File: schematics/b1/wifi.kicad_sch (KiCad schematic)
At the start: 0 parts

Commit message: Updated Wi-Fi block.
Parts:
- added C18: 1 mF, symbol Device:C_Polarized
- added J1: Conn_01x06_Pin, symbol Connector:Conn_01x06_Pin
- added R26, R27, R28, R29, R30: 10k, symbol Device:R
- added SW2, SW3: SW_Push, symbol Switch:SW_Push
- added U6: ESP-12F, RF_Module:ESP-12E, symbol RF_Module:ESP-12F
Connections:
- new net: R27.2, U6.3 (EN)
- new net: R26.1, SW2.2, U6.1 (~{RST})
- new net: J1.4 (TX), U6.21 (GPIO3/RXD)
- new net: J1.5 (RX), U6.22 (GPIO1/TXD)
- new net: R29.1, U6.17 (GPIO2)
- new net CS: R30.1, U6.16 (GPIO15)
- new net GND: C18.2, J1.1 (GND), R30.2, SW2.1, SW3.1, U6.15 (GND)
- new net GPIO0: R28.2, SW3.2, U6.18 (GPIO0)
- new net GPIO4: U6.19 (GPIO4)
- new net GPIO5: U6.20 (GPIO5)
- new net MOSI: U6.7 (GPIO13)
- new net SCLK: U6.5 (GPIO14)
- new net VCC: C18.1, R26.2, R27.1, R28.1, R29.2, U6.8 (VCC)
- no-connect marks 0 -> 12
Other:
- note added: "An extremely beefy capacitor is needed so that VCC doesn't drop too low at boot time, or else the ESP-12F will crash and enter an idle state."
- note added: "If this is held down while the module is booting, then it will enter flash mode."
- note added: "If this is pushed, then the module will reset."

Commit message: Updated index page.
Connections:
- net RX: now reaches J1.4 (TX), U6.21 (GPIO3/RXD)
- net TX: now reaches J1.5 (RX), U6.22 (GPIO1/TXD)
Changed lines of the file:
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@@
     (comment 3 "A B1 (Badger One) node is the core hardware unit of the Badger sytem. It handles card")
+  )
+  (junction (at 115.57 46.99) (diameter 0) (color 0 0 0 0)
   )
   (junction (at 95.25 34.29) (diameter 0) (color 0 0 0 0)
   )
   (junction (at 137.16 57.15) (diameter 0) (color 0 0 0 0)
+  )
+  (junction (at 113.03 44.45) (diameter 0) (color 0 0 0 0)
   )
   (junction (at 118.11 80.01) (diameter 0) (color 0 0 0 0)
@@
     (stroke (width 0) (type default))
   )
+  (wire (pts (xy 113.03 44.45) (xy 118.11 44.45))
+    (stroke (width 0) (type default))
+  )
   (wire (pts (xy 95.25 34.29) (xy 95.25 52.07))
     (stroke (width 0) (type default))
@@
     (stroke (width 0) (type default))
   )
+  (wire (pts (xy 113.03 44.45) (xy 113.03 36.83))
+    (stroke (width 0) (type default))
+  )
+  (wire (pts (xy 115.57 46.99) (xy 118.11 46.99))
+    (stroke (width 0) (type default))
+  )
   (wire (pts (xy 110.49 59.69) (xy 113.03 59.69))
     (stroke (width 0) (type default))
@@
     (stroke (width 0) (type default))
   )
-  (wire (pts (xy 113.03 59.69) (xy 113.03 36.83))
+  (wire (pts (xy 113.03 59.69) (xy 113.03 44.45))
     (stroke (width 0) (type default))
   )
   (wire (pts (xy 110.49 62.23) (xy 127 62.23))
+    (stroke (width 0) (type default))
+  )
+  (wire (pts (xy 115.57 46.99) (xy 115.57 36.83))
     (stroke (width 0) (type default))
   )
@@
     (stroke (width 0) (type default))
   )
-  (wire (pts (xy 115.57 64.77) (xy 115.57 36.83))
+  (wire (pts (xy 115.57 64.77) (xy 115.57 46.99))
     (stroke (width 0) (type default))
   )
@@
     (effects (font (size 1.27 1.27)) (justify left))
   )
+  (hierarchical_label "TX" (shape output) (at 118.11 44.45 0) (fields_autoplaced)
+    (effects (font (size 1.27 1.27)) (justify left))
+  )
   (hierarchical_label "VCC" (shape input) (at 137.16 48.26 90) (fields_autoplaced)
     (effects (font (size 1.27 1.27)) (justify left))
@@
     (effects (font (size 1.27 1.27)) (justify right))
   )
+  (hierarchical_label "RX" (shape input) (at 118.11 46.99 0) (fields_autoplaced)
+    (effects (font (size 1.27 1.27)) (justify left))
+  )
   (hierarchical_label "MOSI" (shape output) (at 110.49 74.93 0) (fields_autoplaced)

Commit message: Added MCU primary schematic page.
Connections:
- net CS renamed ~{CS}
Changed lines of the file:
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@@
     (rev "1")
     (company "shawnd.xyz")
-    (comment 2 "scanning as well as radio communications and outputs/displays.")
-    (comment 3 "A B1 (Badger One) node is the core hardware unit of the Badger sytem. It handles card")
+    (comment 3 "Wi-Fi networking as well as handling the e-paper display.")
+    (comment 4 "The ESP-12F has an ESP8266 microprocessor and onboard antenna, and handles all")
   )
   (junction (at 115.57 46.99) (diameter 0) (color 0 0 0 0)
@@
     (effects (font (size 1.27 1.27)) (justify right bottom))
   )
-  (hierarchical_label "CS" (shape output) (at 120.65 80.01 0) (fields_autoplaced)
+  (hierarchical_label "~{CS}" (shape output) (at 120.65 80.01 0) (fields_autoplaced)
     (effects (font (size 1.27 1.27)) (justify left))
   )

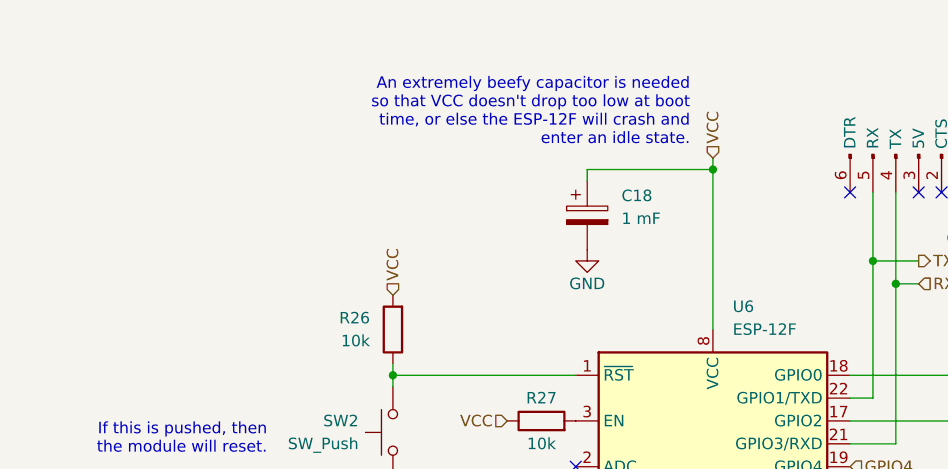
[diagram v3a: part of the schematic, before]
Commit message: Added workaround for ESP-12F boot issue.
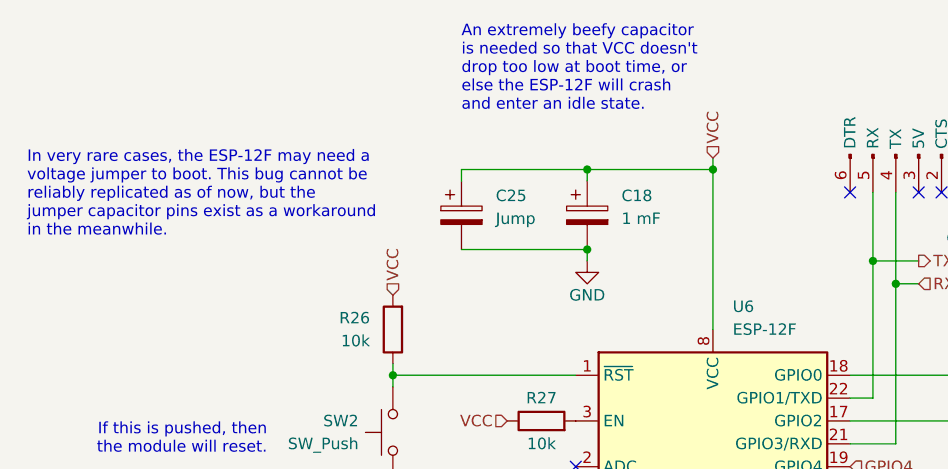
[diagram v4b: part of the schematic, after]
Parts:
- added C25: Jump, symbol Device:C_Polarized
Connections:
- net GND: now also C25.2
- net VCC: now also C25.1
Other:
- note added: "In very rare cases, the ESP-12F may need a voltage jumper to boot. This bug cannot be reliably replicated as of now, but the jumper capacitor pins exist as a workaround in the meanwhile."
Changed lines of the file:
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@@
   (junction (at 115.57 46.99) (diameter 0) (color 0 0 0 0)
   )
+  (junction (at 81.28 34.29) (diameter 0) (color 0 0 0 0)
+  )
   (junction (at 95.25 34.29) (diameter 0) (color 0 0 0 0)
   )
@@
   )
   (junction (at 113.03 44.45) (diameter 0) (color 0 0 0 0)
+  )
+  (junction (at 81.28 43.18) (diameter 0) (color 0 0 0 0)
   )
   (junction (at 118.11 80.01) (diameter 0) (color 0 0 0 0)
@@
     (stroke (width 0) (type default))
   )
+  (wire (pts (xy 67.31 34.29) (xy 67.31 35.56))
+    (stroke (width 0) (type default))
+  )
   (wire (pts (xy 95.25 33.02) (xy 95.25 34.29))
     (stroke (width 0) (type default))
@@
     (stroke (width 0) (type default))
   )
+  (wire (pts (xy 81.28 44.45) (xy 81.28 43.18))
+    (stroke (width 0) (type default))
+  )
   (wire (pts (xy 110.49 80.01) (xy 118.11 80.01))
     (stroke (width 0) (type default))
@@
     (stroke (width 0) (type default))
   )
+  (wire (pts (xy 81.28 34.29) (xy 67.31 34.29))
+    (stroke (width 0) (type default))
+  )
   (wire (pts (xy 115.57 46.99) (xy 115.57 36.83))
     (stroke (width 0) (type default))
@@
     (stroke (width 0) (type default))
   )
+  (wire (pts (xy 67.31 43.18) (xy 81.28 43.18))
+    (stroke (width 0) (type default))
+  )
   (wire (pts (xy 127 62.23) (xy 127 55.88))
     (stroke (width 0) (type default))
   )
-  (text "An extremely beefy capacitor is needed\nso that VCC doesn't drop too low at boot\ntime, or else the ESP-12F will crash and\nenter an idle state."
-    (at 92.71 31.75 0)
-    (effects (font (size 1.27 1.27)) (justify right bottom))
+  (text "In very rare cases, the ESP-12F may need a\nvoltage jumper to boot. This bug cannot be\nreliably replicated as of now, but the\njumper capacitor pins exist as a workaround\nin the meanwhile."
+    (at 19.05 41.91 0)
+    (effects (font (size 1.27 1.27)) (justify left bottom))
+  )
+  (text "An extremely beefy capacitor\nis needed so that VCC doesn't\ndrop too low at boot time, or\nelse the ESP-12F will crash\nand enter an idle state."
+    (at 67.31 27.94 0)
+    (effects (font (size 1.27 1.27)) (justify left bottom))
   )
   (text "If this is held down while\nthe module is booting, then\nit will enter flash mode."
@@
     )
   )
-  (symbol (lib_id "power:GND") (at 81.28 43.18 0) (unit 1)
-    (in_bom yes) (on_board yes) (dnp no)
-    (property "Reference" "#PWR026" (at 81.28 49.53 0)
-      (effects (font (size 1.27 1.27)) hide)
-    )
-    (property "Value" "GND" (at 81.28 46.99 0)
+  (symbol (lib_id "power:GND") (at 81.28 44.45 0) (unit 1)
+    (in_bom yes) (on_board yes) (dnp no)
+    (property "Reference" "#PWR026" (at 81.28 50.8 0)
+      (effects (font (size 1.27 1.27)) hide)
+    )
+    (property "Value" "GND" (at 81.28 48.26 0)
       (effects (font (size 1.27 1.27)))
     )
-    (property "Footprint" "" (at 81.28 43.18 0)
-      (effects (font (size 1.27 1.27)) hide)
-    )
-    (property "Datasheet" "" (at 81.28 43.18 0)
+    (property "Footprint" "" (at 81.28 44.45 0)
+      (effects (font (size 1.27 1.27)) hide)
+    )
+    (property "Datasheet" "" (at 81.28 44.45 0)
       (effects (font (size 1.27 1.27)) hide)
     )
@@
         )
       )
+    )
+  )
+  (symbol (lib_id "Device:C_Polarized") (at 67.31 39.37 0) (unit 1)
+    (in_bom yes) (on_board yes) (dnp no)
+    (property "Reference" "C25" (at 71.12 37.211 0)
+      (effects (font (size 1.27 1.27)) (justify left))
+    )
+    (property "Value" "Jump" (at 71.12 39.751 0)
+      (effects (font (size 1.27 1.27)) (justify left))
+    )
+    (property "Footprint" "" (at 68.2752 43.18 0)
+      (effects (font (size 1.27 1.27)) hide)
+    )
+    (property "Datasheet" "~" (at 67.31 39.37 0)
+      (effects (font (size 1.27 1.27)) hide)
+    )
+    (pin "2")
+    (pin "1")
+    (instances
+      (project "b1"
+        (path "/d6142fa5-2354-4512-9919-37616259c364/a74f58bd-54a1-4bdf-85a5-bb477b4492d8"
+          (reference "C25") (unit 1)
+        )
+      )

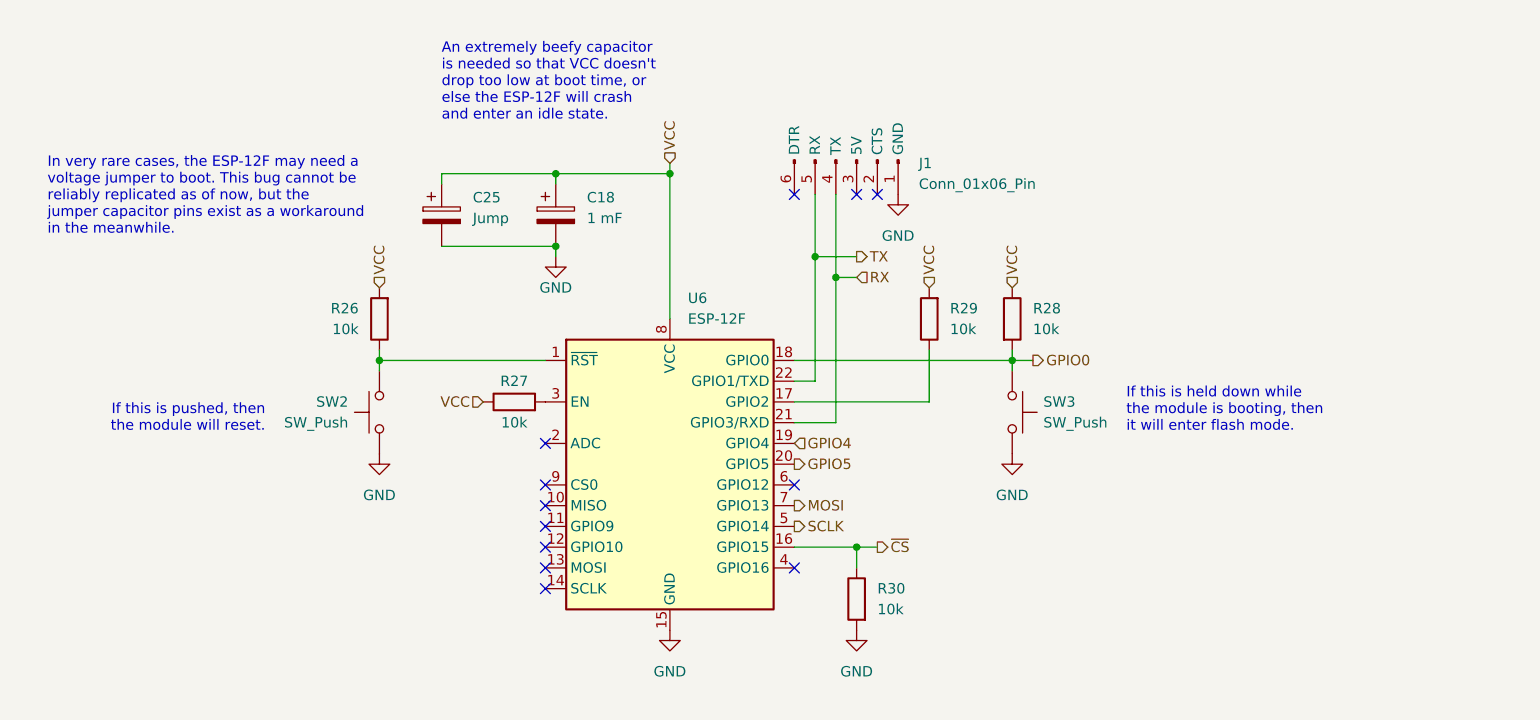
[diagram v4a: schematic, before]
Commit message: Updated Wi-Fi block with a jumper switch as a workaround.
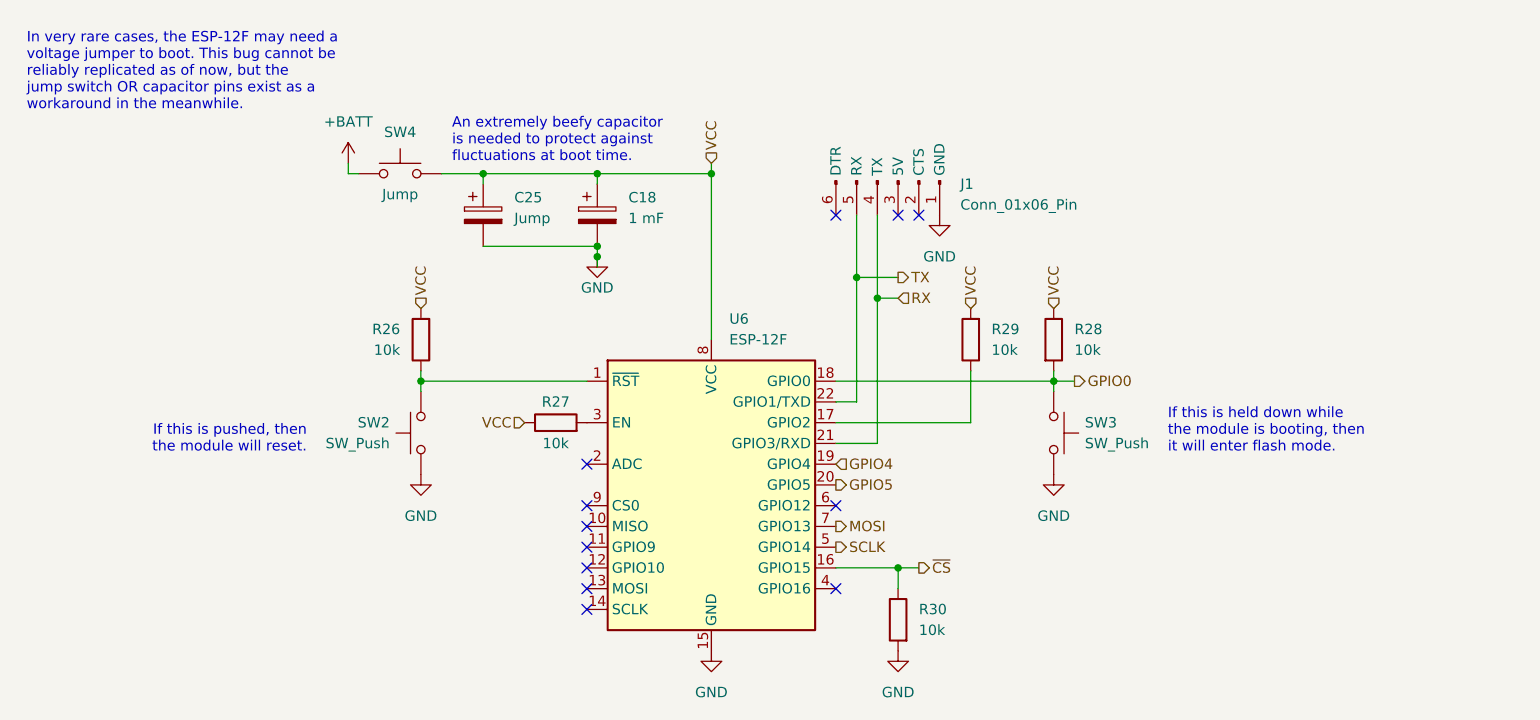
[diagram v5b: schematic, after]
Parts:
- added SW4: Jump, symbol Switch:SW_Push
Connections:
- net VCC: now also SW4.2
- new net +BATT: SW4.1
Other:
- note added: "An extremely beefy capacitor is needed to protect against fluctuations at boot time."
- note added: "In very rare cases, the ESP-12F may need a voltage jumper to boot. This bug cannot be reliably replicated as of now, but the jump switch OR capacitor pins exist as a workaround in the meanwhile."
- note removed: "An extremely beefy capacitor is needed so that VCC doesn't drop too low at boot time, or else the ESP-12F will crash and enter an idle state."
- note removed: "In very rare cases, the ESP-12F may need a voltage jumper to boot. This bug cannot be reliably replicated as of now, but the jumper capacitor pins exist as a workaround in the meanwhile."
- moved on the sheet: C18, C25, J1, R26, R27, R28, R29, R30, SW2, SW3, U6

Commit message: Added instructions for the voltage jumper.
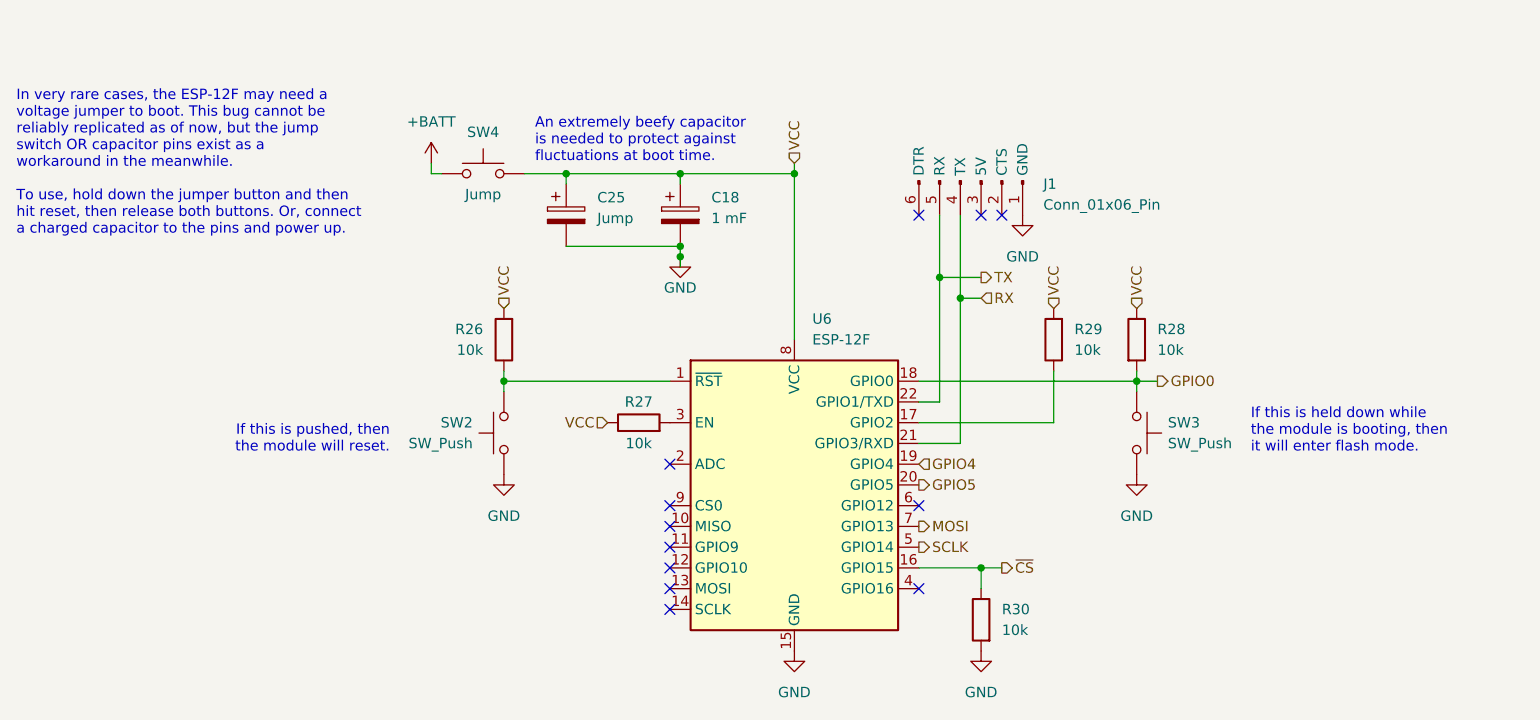
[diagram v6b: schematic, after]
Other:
- note added: "In very rare cases, the ESP-12F may need a voltage jumper to boot. This bug cannot be reliably replicated as of now, but the jump switch OR capacitor pins exist as a workaround in the meanwhile. To use, hold down the jumper button and then hit reset, then release both buttons. Or, connect a charged capacitor to the pins and power up."
- note removed: "In very rare cases, the ESP-12F may need a voltage jumper to boot. This bug cannot be reliably replicated as of now, but the jump switch OR capacitor pins exist as a workaround in the meanwhile."
- moved on the sheet: C18, C25, J1, R26, R27, R28, R29, R30, SW2, SW3, SW4, U6

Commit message: Updated Wi-Fi and MCU schematic.
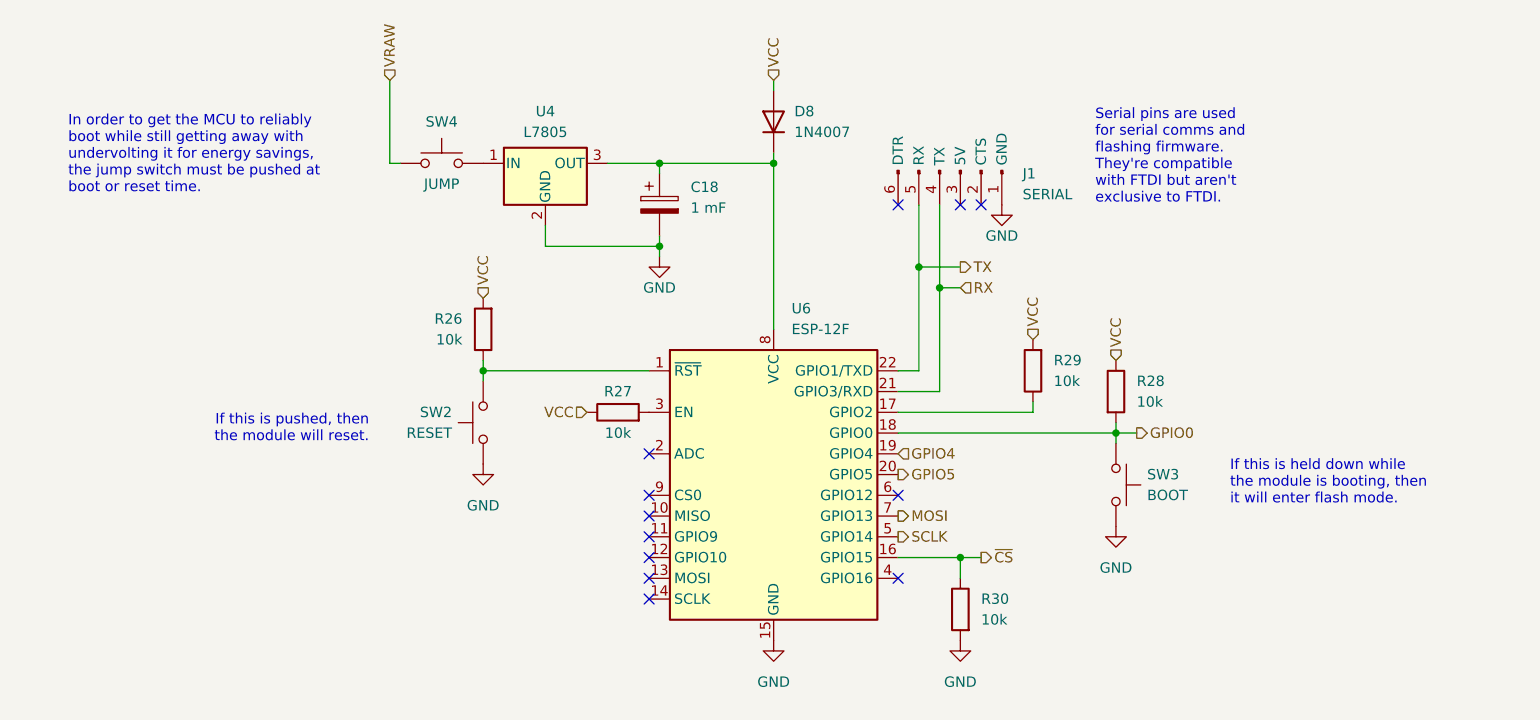
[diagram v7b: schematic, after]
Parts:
- removed C25: Jump, symbol Device:C_Polarized
- added D8: 1N4007, Diode_THT:D_DO-41_SOD81_P10.16mm_Horizontal, symbol Diode:1N4007
- added U4: L7805, symbol Regulator_Linear:L7805
- J1: value Conn_01x06_Pin -> SERIAL
- SW2: value SW_Push -> RESET
- SW3: value SW_Push -> BOOT
- SW4: value Jump -> JUMP
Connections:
- net GND: now also U4.2 (GND)
- net VCC: now also D8.2 (A); no longer C18.1, SW4.2, U6.8 (VCC)
- net +BATT renamed VRAW
- new net: C18.1, D8.1 (K), U4.3 (OUT), U6.8 (VCC)
- new net: SW4.2, U4.1 (IN)
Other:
- note added: "In order to get the MCU to reliably boot while still getting away with undervolting it for energy savings, the jump switch must be pushed at boot or reset time."
- note added: "Serial pins are used for serial comms and flashing firmware. They're compatible with FTDI but aren't exclusive to FTDI."
- note removed: "An extremely beefy capacitor is needed to protect against fluctuations at boot time."
- note removed: "In very rare cases, the ESP-12F may need a voltage jumper to boot. This bug cannot be reliably replicated as of now, but the jump switch OR capacitor pins exist as a workaround in the meanwhile. To use, hold down the jumper button and then hit reset, then release both buttons. Or, connect a charged capacitor to the pins and power up."
- moved on the sheet: C18, J1, R26, R27, R28, R29, R30, SW2, SW3, U6
